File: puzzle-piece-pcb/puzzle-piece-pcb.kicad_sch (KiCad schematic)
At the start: 7 parts, among them J1 OLED, J2 Input, J3 PROG_DEBUG, U1 ATtiny1624-SS

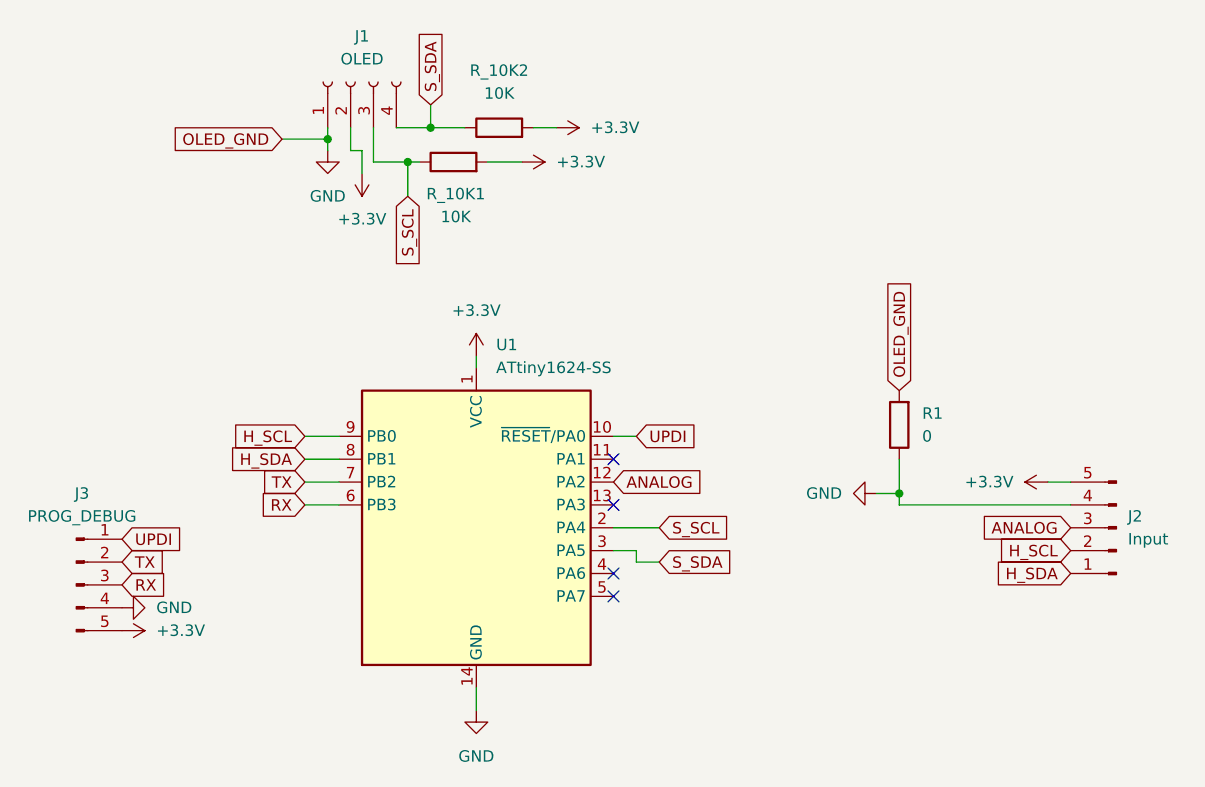
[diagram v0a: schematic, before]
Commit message: made battery controller singled sided and removed lipo
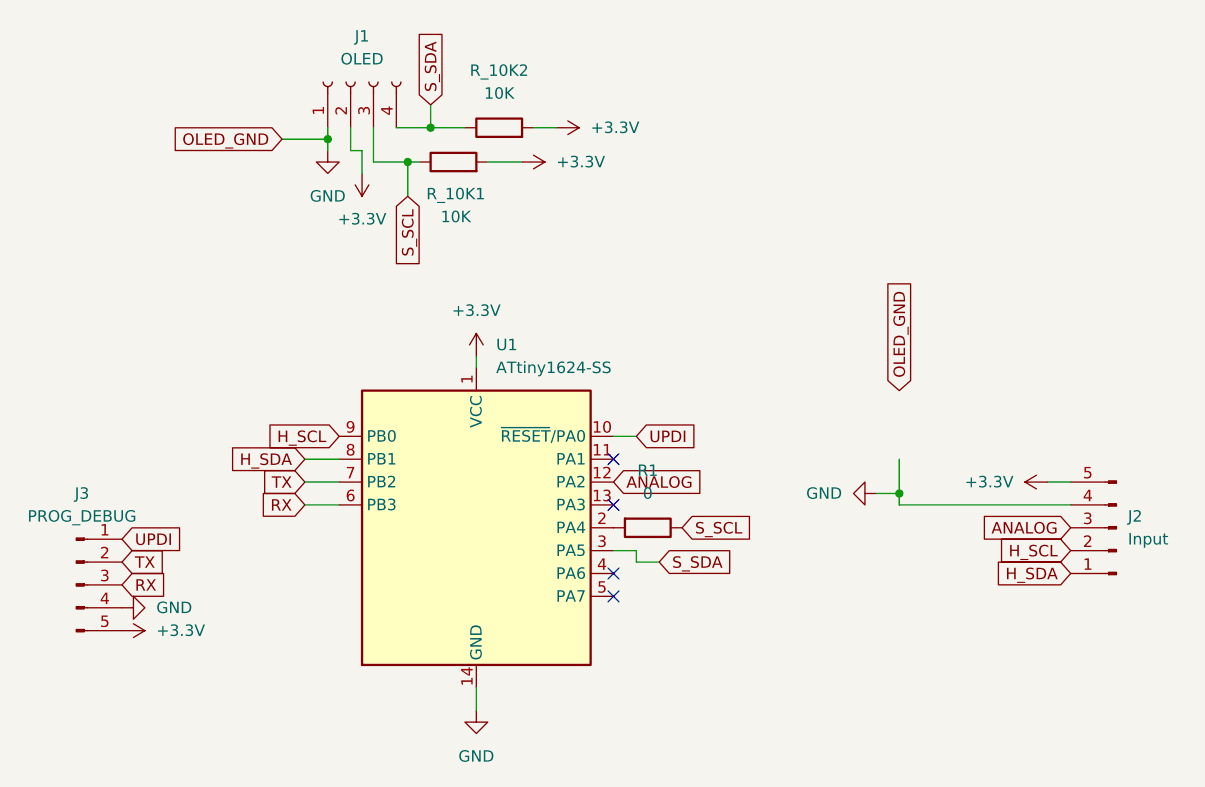
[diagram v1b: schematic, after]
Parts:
- J2, J3: footprint Connector_PinHeader_2.54mm:PinHeader_1x05_P2.54mm_Vertical -> Connector_PinSocket_2.54mm:PinSocket_1x05_P2.54mm_Vertical_SMD_Pin1Left
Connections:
- net GND: no longer R1.1, R1.2
- net S_SCL: now also R1.1; no longer U1.2 (PA4)
- new net: R1.2, U1.2 (PA4)
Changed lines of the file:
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@@
-	(wire
-		(pts
-			(xy 157.48 110.49) (xy 162.56 110.49)
-		)
-		(stroke
-			(width 0)
-			(type default)
-		)
-	)
-	(wire
-		(pts
-			(xy 123.19 100.33) (xy 127 100.33)
-		)
-		(stroke
-			(width 0)
-			(type default)
-		)
-	)
 	(wire
 		(pts
@@
 	(global_label "H_SCL"
 		(shape input)
-		(at 123.19 100.33 180)
+		(at 127 100.33 180)
 		(fields_autoplaced yes)
 		(effects
@@
 		)
 		(property "Intersheetrefs" "${INTERSHEET_REFS}"
-			(at 114.3991 100.33 0)
+			(at 118.2091 100.33 0)
 			(effects
 				(font
@@
 	(global_label "S_SCL"
 		(shape input)
-		(at 162.56 110.49 0)
+		(at 165.1 110.49 0)
 		(fields_autoplaced yes)
 		(effects
@@
 		)
 		(property "Intersheetrefs" "${INTERSHEET_REFS}"
-			(at 171.2299 110.49 0)
+			(at 173.7699 110.49 0)
 			(effects
 				(font
@@
 				(justify right)
 				(hide yes)
+			)
+		)
+	)
+	(symbol
+		(lib_id "Device:R")
+		(at 161.29 110.49 270)
+		(unit 1)
+		(exclude_from_sim no)
+		(in_bom yes)
+		(on_board yes)
+		(dnp no)
+		(fields_autoplaced yes)
+		(property "Reference" "R1"
+			(at 161.29 104.14 90)
+			(effects
+				(font
+					(size 1.27 1.27)
+				)
+			)
+		)
+		(property "Value" "0"
+			(at 161.29 106.68 90)
+			(effects
+				(font
+					(size 1.27 1.27)
+				)
+			)
+		)
+		(property "Footprint" "Resistor_SMD:R_1206_3216Metric"
+			(at 161.29 108.712 90)
+			(effects
+				(font
+					(size 1.27 1.27)
+				)
+				(hide yes)
+			)
+		)
+		(property "Datasheet" "~"
+			(at 161.29 110.49 0)
+			(effects
+				(font
+					(size 1.27 1.27)
+				)
+				(hide yes)
+			)
+		)
+		(property "Description" "Resistor"
+			(at 161.29 110.49 0)
+			(effects
+				(font
+					(size 1.27 1.27)
+				)
+				(hide yes)
+			)
+		)
+		(pin "1"
+		)
+		(pin "2"
+		)
+		(instances
+			(project "puzzle-piece-pcb"
+				(path "/a892464e-fb25-4684-a99d-b733cb33a109"
+					(reference "R1")
+					(unit 1)
+				)
 			)
 		)
@@
 			)
 		)
-		(property "Footprint" "Connector_PinHeader_2.54mm:PinHeader_1x05_P2.54mm_Vertical"
+		(property "Footprint" "Connector_PinSocket_2.54mm:PinSocket_1x05_P2.54mm_Vertical_SMD_Pin1Left"
 			(at 97.79 116.84 0)
 			(effects
@@
 			)
 		)
-		(property "Footprint" "Connector_PinHeader_2.54mm:PinHeader_1x05_P2.54mm_Vertical"
+		(property "Footprint" "Connector_PinSocket_2.54mm:PinSocket_1x05_P2.54mm_Vertical_SMD_Pin1Left"
 			(at 213.36 110.49 0)
 			(effects
@@
 					(unit 1)
 				)
-			)
-		)
-	)
-	(symbol
-		(lib_id "Device:R")
-		(at 189.23 99.06 180)
-		(unit 1)
-		(exclude_from_sim no)
-		(in_bom yes)
-		(on_board yes)
-		(dnp no)
-		(fields_autoplaced yes)
-		(property "Reference" "R1"
-			(at 191.77 97.7899 0)
-			(effects
-				(font
-					(size 1.27 1.27)
-				)
-				(justify right)
-			)
-		)
-		(property "Value" "0"
-			(at 191.77 100.3299 0)
-			(effects
-				(font
-					(size 1.27 1.27)
-				)
-				(justify right)
-			)
-		)
-		(property "Footprint" "Resistor_SMD:R_1206_3216Metric"
-			(at 191.008 99.06 90)
-			(effects
-				(font
-					(size 1.27 1.27)
-				)
-				(hide yes)
-			)
-		)
-		(property "Datasheet" "~"
-			(at 189.23 99.06 0)
-			(effects
-				(font
-					(size 1.27 1.27)
-				)
-				(hide yes)
-			)
-		)
-		(property "Description" "Resistor"
-			(at 189.23 99.06 0)
-			(effects
-				(font
-					(size 1.27 1.27)
-				)
-				(hide yes)
-			)
-		)
-		(pin "1"
-		)
-		(pin "2"
-		)
-		(instances
-			(project ""
-				(path "/a892464e-fb25-4684-a99d-b733cb33a109"
-					(reference "R1")
-					(unit 1)
-				)
